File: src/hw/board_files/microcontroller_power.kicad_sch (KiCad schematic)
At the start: 33 parts, among them J2 JST S3B-PH-K-S, J3 Conn_ARM_SWD_TagConnect_TC203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, SW1 RESET, SW2 SW_PWR, U3 BQ24074RGT, U4 MDBT50Q-1MV2, U5 XC6220B331MR, U6 W25Q32JVSS, Y2 32.768kHz

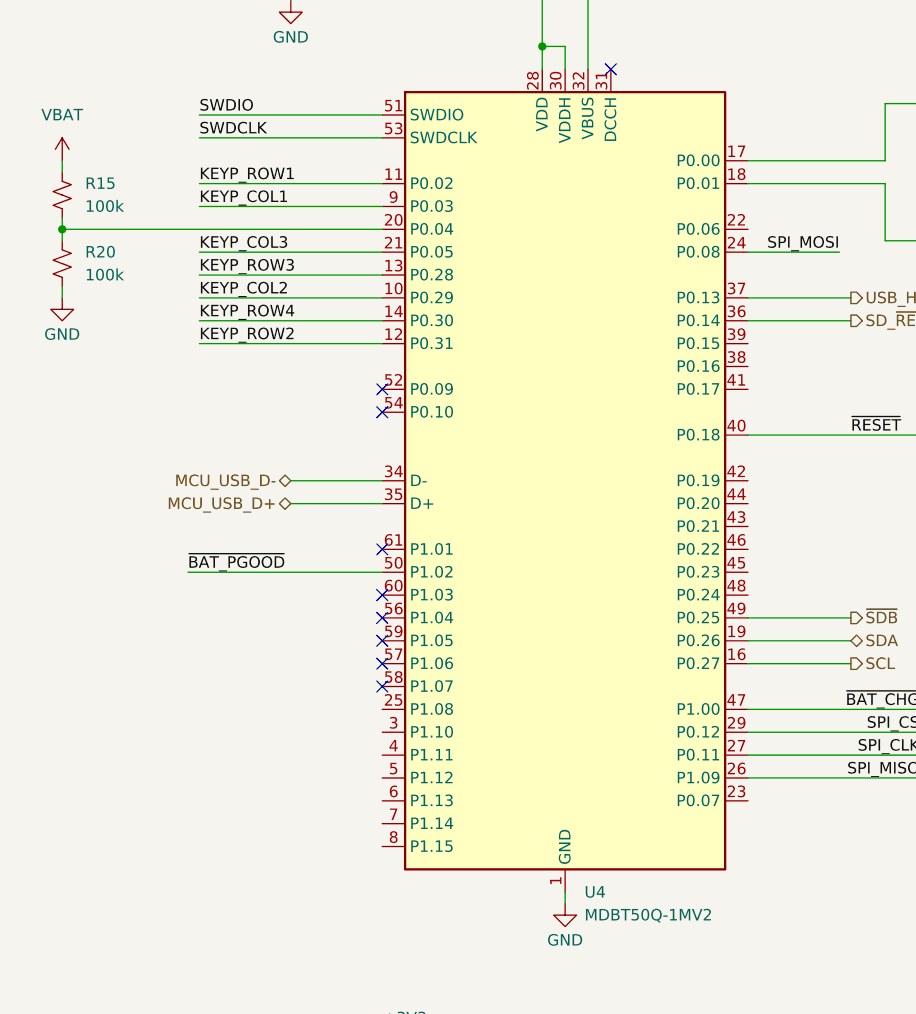
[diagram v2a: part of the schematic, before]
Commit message: Added rotary encoder and OLED. Started laying out board then I need to review schematic and change pinout if needed
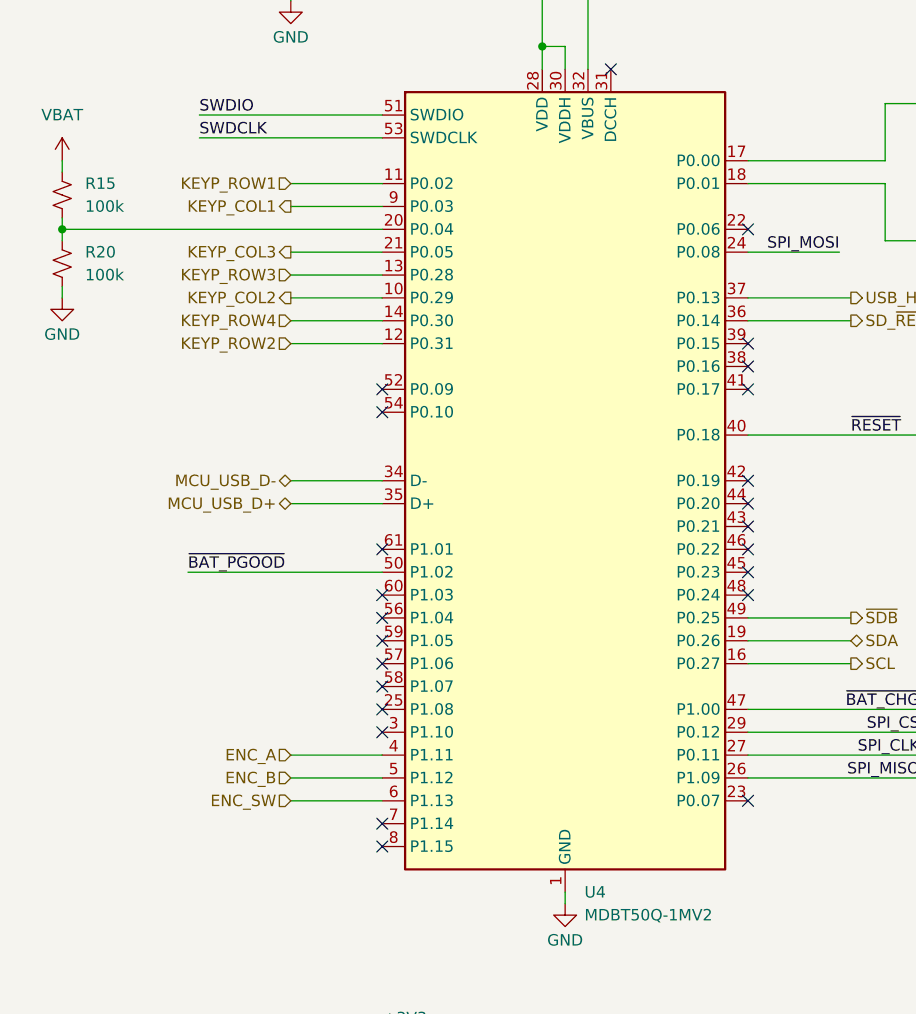
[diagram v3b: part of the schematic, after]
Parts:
- R11, R12, R13, R14, R16, R17, R18, R19, R21, R22: footprint Resistor_SMD:R_0805_2012Metric_Pad1.20x1.40mm_HandSolder -> Resistor_SMD:R_0603_1608Metric_Pad0.98x0.95mm_HandSolder
- R15, R20: footprint Resistor_SMD:R_0603_1608Metric_Pad0.98x0.95mm_HandSolder -> Resistor_SMD:R_0805_2012Metric_Pad1.20x1.40mm_HandSolder
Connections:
- net ENC_A: now reaches U4.4 (P1.11)
- net ENC_B: now reaches U4.5 (P1.12)
- net ENC_SW: now reaches U4.6 (P1.13)
- no-connect marks 11 -> 26
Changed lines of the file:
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@@
 	)
 	(no_connect
+		(at 92.71 116.84)
+	)
+	(no_connect
+		(at 92.71 114.3)
+	)
+	(no_connect
+		(at 92.71 139.7)
+	)
+	(no_connect
+		(at 92.71 93.98)
+	)
+	(no_connect
+		(at 52.07 129.54)
+	)
+	(no_connect
+		(at 92.71 76.2)
+	)
+	(no_connect
+		(at 52.07 142.24)
+	)
+	(no_connect
 		(at 52.07 111.76)
 	)
@@
 	)
 	(no_connect
+		(at 52.07 132.08)
+	)
+	(no_connect
 		(at 52.07 121.92)
 	)
 	(no_connect
+		(at 92.71 104.14)
+	)
+	(no_connect
+		(at 92.71 109.22)
+	)
+	(no_connect
 		(at 52.07 96.52)
 	)
 	(no_connect
+		(at 92.71 111.76)
+	)
+	(no_connect
 		(at 52.07 116.84)
 	)
@@
 	)
 	(no_connect
+		(at 92.71 91.44)
+	)
+	(no_connect
+		(at 92.71 106.68)
+	)
+	(no_connect
 		(at 64.77 185.42)
 	)
@@
 	)
 	(no_connect
+		(at 92.71 88.9)
+	)
+	(no_connect
 		(at 77.47 58.42)
 	)
@@
 	)
 	(no_connect
+		(at 52.07 144.78)
+	)
+	(no_connect
 		(at 52.07 124.46)
 	)
@@
 	(wire
 		(pts
-			(xy 31.75 83.82) (xy 52.07 83.82)
+			(xy 41.91 83.82) (xy 52.07 83.82)
 		)
 		(stroke
@@
 	(wire
 		(pts
-			(xy 31.75 71.12) (xy 52.07 71.12)
+			(xy 41.91 71.12) (xy 52.07 71.12)
 		)
 		(stroke
@@
 	(wire
 		(pts
+			(xy 41.91 139.7) (xy 52.07 139.7)
+		)
+		(stroke
+			(width 0)
+			(type default)
+		)
+	)
+	(wire
+		(pts
 			(xy 133.35 69.85) (xy 133.35 71.12)
 		)
@@
 	(wire
 		(pts
-			(xy 31.75 88.9) (xy 52.07 88.9)
+			(xy 41.91 88.9) (xy 52.07 88.9)
 		)
 		(stroke
@@
 	(wire
 		(pts
-			(xy 31.75 73.66) (xy 52.07 73.66)
+			(xy 41.91 73.66) (xy 52.07 73.66)
 		)
 		(stroke
@@
 	(wire
 		(pts
-			(xy 31.75 78.74) (xy 52.07 78.74)
+			(xy 41.91 78.74) (xy 52.07 78.74)
 		)
 		(stroke
@@
 	(wire
 		(pts
-			(xy 31.75 86.36) (xy 52.07 86.36)
+			(xy 41.91 86.36) (xy 52.07 86.36)
 		)
 		(stroke
@@
 	(wire
 		(pts
-			(xy 31.75 81.28) (xy 52.07 81.28)
+			(xy 41.91 81.28) (xy 52.07 81.28)
+		)
+		(stroke
+			(width 0)
+			(type default)
+		)
+	)
+	(wire
+		(pts
+			(xy 41.91 134.62) (xy 52.07 134.62)
 		)
 		(stroke
@@
 		)
 	)
+	(wire
+		(pts
+			(xy 41.91 137.16) (xy 52.07 137.16)
+		)
+		(stroke
+			(width 0)
+			(type default)
+		)
+	)
 	(label "SPI_CS"
 		(at 111.76 132.08 180)
@@
 		)
 	)
-	(label "KEYP_COL1"
-		(at 31.75 73.66 0)
-		(effects
-			(font
-				(size 1.27 1.27)
-			)
-			(justify left bottom)
-		)
-	)
 	(label "SPI_CS"
 		(at 115.57 166.37 0)
@@
 		)
 	)
-	(label "KEYP_ROW4"
-		(at 31.75 86.36 0)
-		(effects
-			(font
-				(size 1.27 1.27)
-			)
-			(justify left bottom)
-		)
-	)
 	(label "~{RESET}"
 		(at 104.14 99.06 0)
@@
 		)
 	)
-	(label "KEYP_ROW1"
-		(at 31.75 71.12 0)
-		(effects
-			(font
-				(size 1.27 1.27)
-			)
-			(justify left bottom)
-		)
-	)
-	(label "KEYP_COL3"
-		(at 31.75 78.74 0)
-		(effects
-			(font
-				(size 1.27 1.27)
-			)
-			(justify left bottom)
-		)
-	)
 	(label "~{BAT_CHG}"
 		(at 214.63 78.74 0)
@@
 		)
 	)
-	(label "KEYP_COL2"
-		(at 31.75 83.82 0)
+	(label "~{BAT_PGOOD}"
+		(at 30.48 114.3 0)
 		(effects
 			(font
@@
 		)
 	)
-	(label "KEYP_ROW3"
-		(at 31.75 81.28 0)
+	(hierarchical_label "SCL"
+		(shape output)
+		(at 104.14 124.46 0)
 		(effects
 			(font
 				(size 1.27 1.27)
 			)
-			(justify left bottom)
+			(justify left)
 		)
 	)
-	(label "KEYP_ROW2"
-		(at 31.75 88.9 0)
+	(hierarchical_label "KEYP_ROW2"
+		(shape input)
+		(at 41.91 88.9 180)
 		(effects
 			(font
 				(size 1.27 1.27)
 			)
-			(justify left bottom)
+			(justify right)
 		)
 	)
-	(label "~{BAT_PGOOD}"
-		(at 30.48 114.3 0)
+	(hierarchical_label "KEYP_COL3"
+		(shape output)
+		(at 41.91 78.74 180)
 		(effects
 			(font
 				(size 1.27 1.27)
 			)
-			(justify left bottom)
+			(justify right)
 		)
 	)
-	(hierarchical_label "SCL"
+	(hierarchical_label "~{SDB}"
 		(shape output)
-		(at 104.14 124.46 0)
+		(at 104.14 119.38 0)
 		(effects
 			(font
@@
 		)
 	)
-	(hierarchical_label "~{SDB}"
-		(shape output)
-		(at 104.14 119.38 0)
+	(hierarchical_label "ENC_SW"
+		(shape input)
+		(at 41.91 139.7 180)
 		(effects
 			(font
 				(size 1.27 1.27)
 			)
-			(justify left)
+			(justify right)
+		)
+	)
+	(hierarchical_label "KEYP_ROW3"
+		(shape input)
+		(at 41.91 81.28 180)
+		(effects
+			(font
+				(size 1.27 1.27)
+			)
+			(justify right)
+		)
+	)
+	(hierarchical_label "KEYP_ROW4"
+		(shape input)
+		(at 41.91 86.36 180)
+		(effects
+			(font
+				(size 1.27 1.27)
+			)
+			(justify right)
 		)
 	)
@@
 		)
 	)
+	(hierarchical_label "ENC_A"
+		(shape input)
+		(at 41.91 134.62 180)
+		(effects
+			(font
+				(size 1.27 1.27)
+			)
+			(justify right)
+		)
+	)
 	(hierarchical_label "USB_HUB_~{RESET}"
 		(shape output)
@@
 		)
 	)
+	(hierarchical_label "ENC_B"
+		(shape input)
+		(at 41.91 137.16 180)
+		(effects
+			(font
+				(size 1.27 1.27)
+			)
+			(justify right)
+		)
+	)
+	(hierarchical_label "KEYP_ROW1"
+		(shape input)
+		(at 41.91 71.12 180)
+		(effects
+			(font
+				(size 1.27 1.27)
+			)
+			(justify right)
+		)
+	)
 	(hierarchical_label "MCU_USB_D+"
 		(shape bidirectional)
@@
 		)
 	)
+	(hierarchical_label "KEYP_COL1"
+		(shape output)
+		(at 41.91 73.66 180)
+		(effects
+			(font
+				(size 1.27 1.27)
+			)
+			(justify right)
+		)
+	)
+	(hierarchical_label "KEYP_COL2"
+		(shape output)
+		(at 41.91 83.82 180)
+		(effects
+			(font
+				(size 1.27 1.27)
+			)
+			(justify right)
+		)
+	)
 	(symbol
 		(lib_id "Device:C_Small")
@@
 			)
 		)
-		(property "Footprint" "Resistor_SMD:R_0805_2012Metric_Pad1.20x1.40mm_HandSolder"
+		(property "Footprint" "Resistor_SMD:R_0603_1608Metric_Pad0.98x0.95mm_HandSolder"
 			(at 163.83 58.42 0)
 			(effects
@@
 			)
 		)
-		(property "Footprint" "Resistor_SMD:R_0805_2012Metric_Pad1.20x1.40mm_HandSolder"
+		(property "Footprint" "Resistor_SMD:R_0603_1608Metric_Pad0.98x0.95mm_HandSolder"
 			(at 133.35 92.71 0)
 			(effects
@@
 			)
 		)
-		(property "Footprint" "Resistor_SMD:R_0805_2012Metric_Pad1.20x1.40mm_HandSolder"
+		(property "Footprint" "Resistor_SMD:R_0603_1608Metric_Pad0.98x0.95mm_HandSolder"
 			(at 229.87 76.2 0)
 			(effects
@@
 			)
 		)
-		(property "Footprint" "Resistor_SMD:R_0805_2012Metric_Pad1.20x1.40mm_HandSolder"
+		(property "Footprint" "Resistor_SMD:R_0603_1608Metric_Pad0.98x0.95mm_HandSolder"
 			(at 181.61 71.12 0)
 			(effects
@@
 			)
 		)
-		(property "Footprint" "Resistor_SMD:R_0805_2012Metric_Pad1.20x1.40mm_HandSolder"
+		(property "Footprint" "Resistor_SMD:R_0603_1608Metric_Pad0.98x0.95mm_HandSolder"
 			(at 163.83 78.74 0)
 			(effects
@@
 			)
 		)
-		(property "Footprint" "Resistor_SMD:R_0603_1608Metric_Pad0.98x0.95mm_HandSolder"
+		(property "Footprint" "Resistor_SMD:R_0805_2012Metric_Pad1.20x1.40mm_HandSolder"
 			(at 16.51 80.01 0)
 			(effects
@@
 			)
 		)
-		(property "Footprint" "Resistor_SMD:R_0805_2012Metric_Pad1.20x1.40mm_HandSolder"
+		(property "Footprint" "Resistor_SMD:R_0603_1608Metric_Pad0.98x0.95mm_HandSolder"
 			(at 181.61 68.58 0)
 			(effects
@@
 			)
 		)
-		(property "Footprint" "Resistor_SMD:R_0805_2012Metric_Pad1.20x1.40mm_HandSolder"
+		(property "Footprint" "Resistor_SMD:R_0603_1608Metric_Pad0.98x0.95mm_HandSolder"
 			(at 229.87 78.74 0)
 			(effects
@@
 			)
 		)
-		(property "Footprint" "Resistor_SMD:R_0805_2012Metric_Pad1.20x1.40mm_HandSolder"
+		(property "Footprint" "Resistor_SMD:R_0603_1608Metric_Pad0.98x0.95mm_HandSolder"
 			(at 163.83 76.2 0)
 			(effects
@@
 			)
 		)
-		(property "Footprint" "Resistor_SMD:R_0603_1608Metric_Pad0.98x0.95mm_HandSolder"
+		(property "Footprint" "Resistor_SMD:R_0805_2012Metric_Pad1.20x1.40mm_HandSolder"
 			(at 16.51 72.39 0)
 			(effects
@@
 			)
 		)
-		(property "Footprint" "Resistor_SMD:R_0805_2012Metric_Pad1.20x1.40mm_HandSolder"
+		(property "Footprint" "Resistor_SMD:R_0603_1608Metric_Pad0.98x0.95mm_HandSolder"
 			(at 163.83 66.04 0)
 			(effects
@@
 			)
 		)
-		(property "Footprint" "Resistor_SMD:R_0805_2012Metric_Pad1.20x1.40mm_HandSolder"
+		(property "Footprint" "Resistor_SMD:R_0603_1608Metric_Pad0.98x0.95mm_HandSolder"
 			(at 128.27 152.4 0)
 			(effects
